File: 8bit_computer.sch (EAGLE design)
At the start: 48 parts, among them IC1 74LS32N, IC10 74LS04N, IC11 74LS04N, IC12 74LS04N, IC13 74LS04N, IC14 74LS08N, IC15 74LS32N, IC16 74LS04N, IC17 74LS86N, IC18 74LS86N, IC19 74LS32N, IC2 74LS04N, IC21 74LS08N, IC22 74LS08N, IC23 74LS32N, IC25 74LS08N, IC26 74LS32N, IC3 74LS08N, IC32 74LS08N, IC33 74LS32N, IC34 74LS245N, IC4 74LS08N, IC5 74LS32N, IC6 74LS04N, IC7 74LS08N, IC8 74LS32N, IC9 74LS04N, Q1 BC556, Q2 BS170

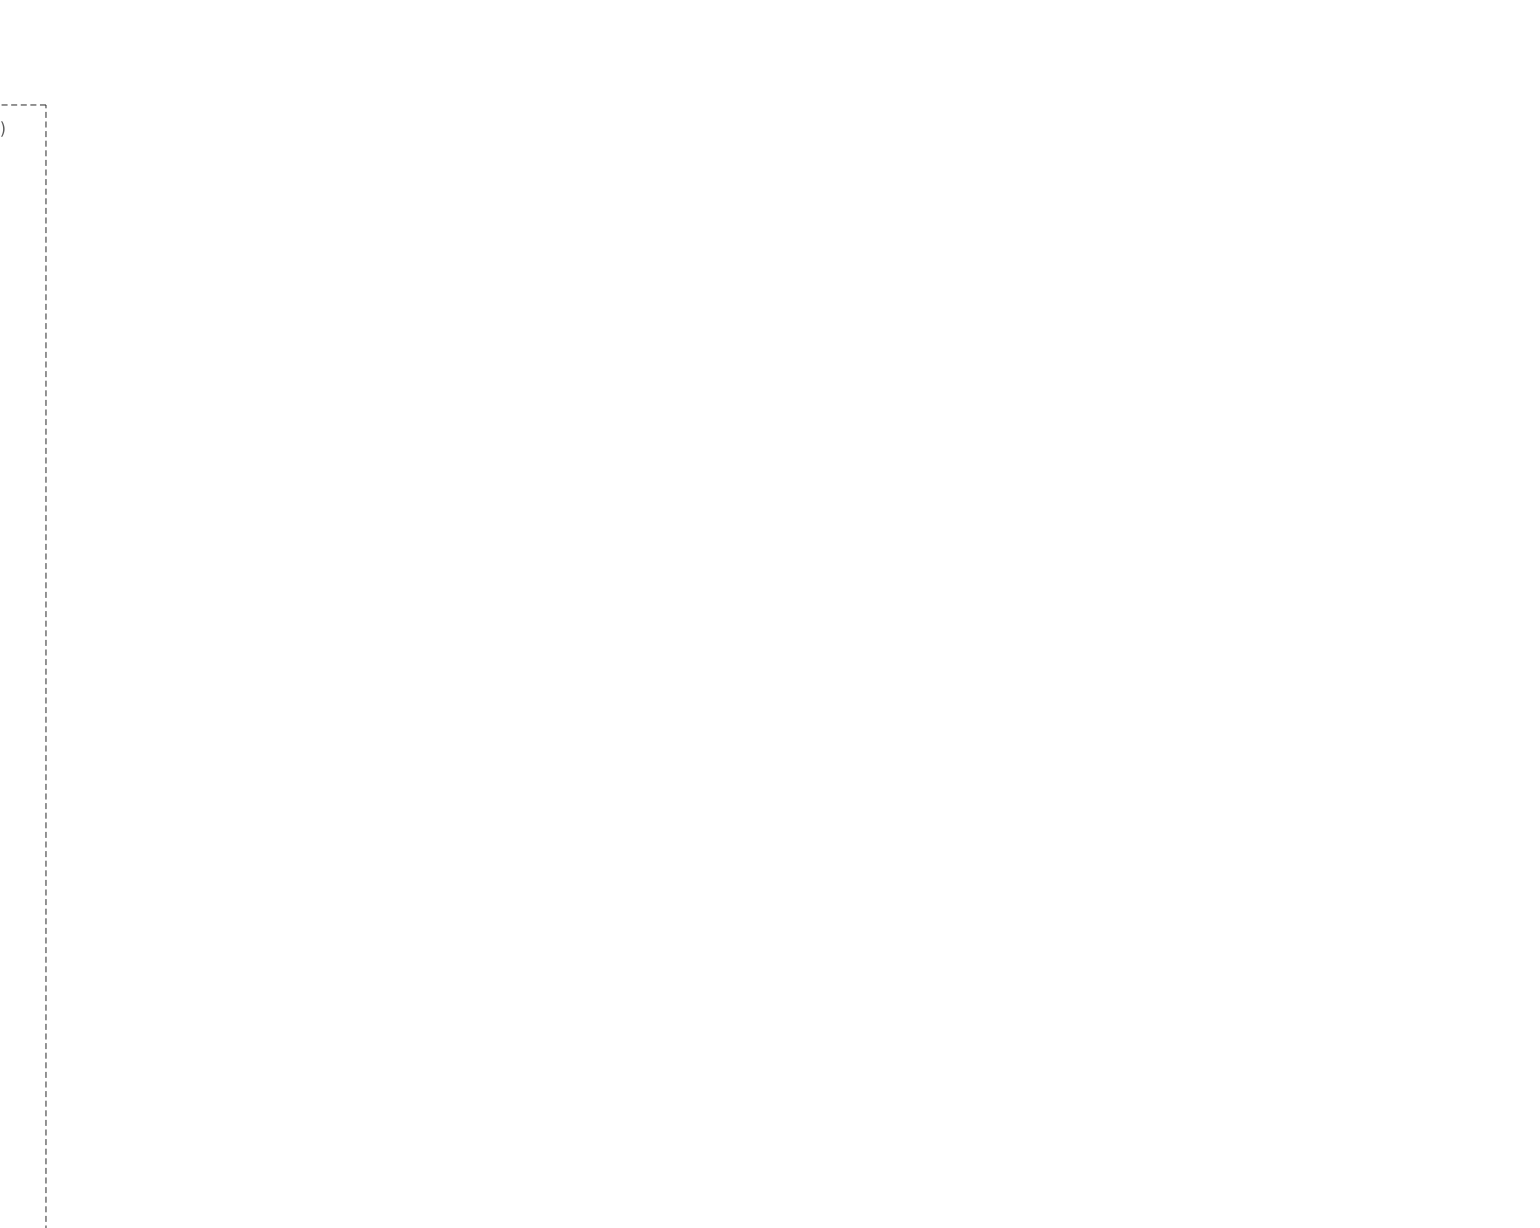
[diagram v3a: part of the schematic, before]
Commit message: Added initial version of SRAM circuit
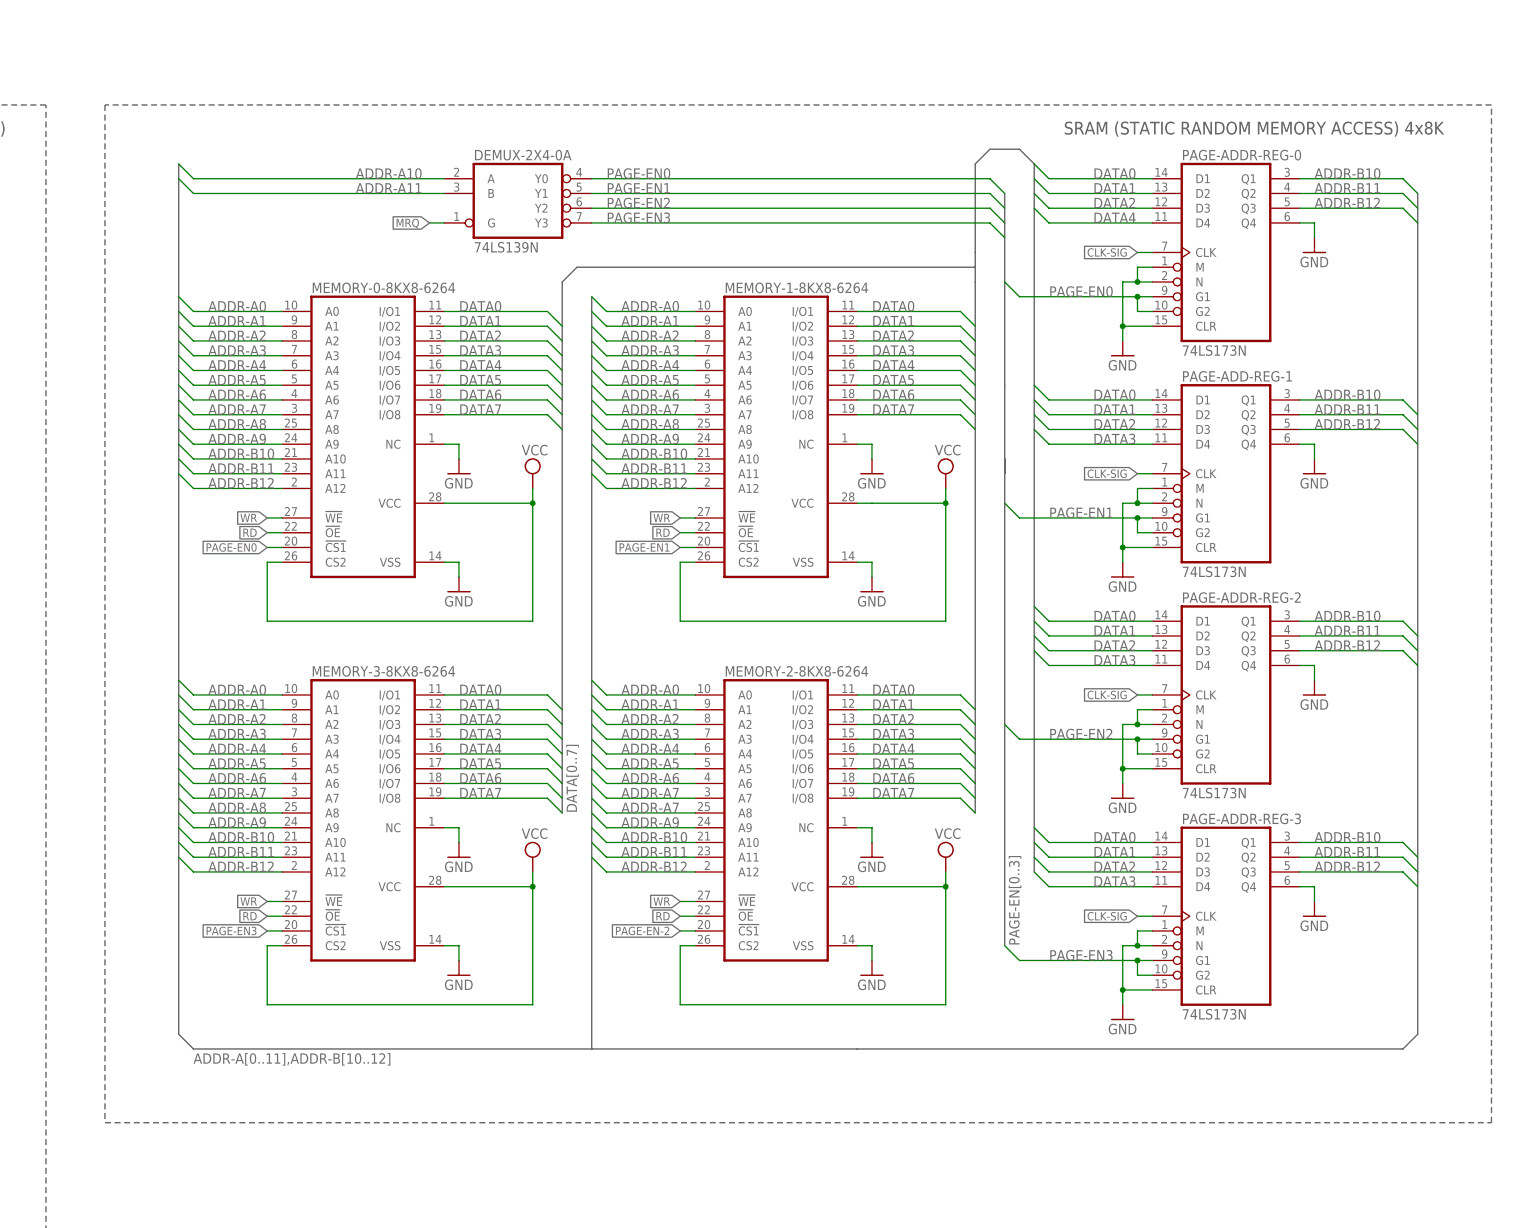
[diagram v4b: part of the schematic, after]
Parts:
- added DEMUX-2X4-0: 74LS139N, 74xx-eu:74LS139N
- added MEMORY-0-8KX8-6264, MEMORY-1-8KX8-6264, MEMORY-2-8KX8-6264, MEMORY-3-8KX8-6264: (no value), memory-hitachi:6264A
- added PAGE-ADD-REG-1, PAGE-ADDR-REG-0, PAGE-ADDR-REG-2, PAGE-ADDR-REG-3: 74LS173N, 74xx-eu:74LS173N
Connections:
- new net ADDR-A0: MEMORY-0-8KX8-6264.A0, MEMORY-1-8KX8-6264.A0, MEMORY-2-8KX8-6264.A0, MEMORY-3-8KX8-6264.A0
- new net ADDR-A1: MEMORY-0-8KX8-6264.A1, MEMORY-1-8KX8-6264.A1, MEMORY-2-8KX8-6264.A1, MEMORY-3-8KX8-6264.A1
- new net ADDR-A10: DEMUX-2X4-0A.A
- new net ADDR-A11: DEMUX-2X4-0A.B
- new net ADDR-A2: MEMORY-0-8KX8-6264.A2, MEMORY-1-8KX8-6264.A2, MEMORY-2-8KX8-6264.A2, MEMORY-3-8KX8-6264.A2
- new net ADDR-A3: MEMORY-0-8KX8-6264.A3, MEMORY-1-8KX8-6264.A3, MEMORY-2-8KX8-6264.A3, MEMORY-3-8KX8-6264.A3
- new net ADDR-A4: MEMORY-0-8KX8-6264.A4, MEMORY-1-8KX8-6264.A4, MEMORY-2-8KX8-6264.A4, MEMORY-3-8KX8-6264.A4
- new net ADDR-A5: MEMORY-0-8KX8-6264.A5, MEMORY-1-8KX8-6264.A5, MEMORY-2-8KX8-6264.A5, MEMORY-3-8KX8-6264.A5
- new net ADDR-A6: MEMORY-0-8KX8-6264.A6, MEMORY-1-8KX8-6264.A6, MEMORY-2-8KX8-6264.A6, MEMORY-3-8KX8-6264.A6
- new net ADDR-A7: MEMORY-0-8KX8-6264.A7, MEMORY-1-8KX8-6264.A7, MEMORY-2-8KX8-6264.A7, MEMORY-2-8KX8-6264.A8, MEMORY-3-8KX8-6264.A7
- new net ADDR-A8: MEMORY-0-8KX8-6264.A8, MEMORY-1-8KX8-6264.A8, MEMORY-3-8KX8-6264.A8
- new net ADDR-A9: MEMORY-0-8KX8-6264.A9, MEMORY-1-8KX8-6264.A9, MEMORY-2-8KX8-6264.A9, MEMORY-3-8KX8-6264.A9
- new net ADDR-B10: MEMORY-0-8KX8-6264.A10, MEMORY-1-8KX8-6264.A10, MEMORY-2-8KX8-6264.A10, MEMORY-3-8KX8-6264.A10, PAGE-ADD-REG-1A.Q1, PAGE-ADDR-REG-0A.Q1, PAGE-ADDR-REG-2A.Q1, PAGE-ADDR-REG-3A.Q1
- new net ADDR-B11: MEMORY-0-8KX8-6264.A11, MEMORY-1-8KX8-6264.A11, MEMORY-2-8KX8-6264.A11, MEMORY-3-8KX8-6264.A11, PAGE-ADD-REG-1A.Q2, PAGE-ADDR-REG-0A.Q2, PAGE-ADDR-REG-2A.Q2, PAGE-ADDR-REG-3A.Q2
- new net ADDR-B12: MEMORY-0-8KX8-6264.A12, MEMORY-1-8KX8-6264.A12, MEMORY-2-8KX8-6264.A12, MEMORY-3-8KX8-6264.A12, PAGE-ADD-REG-1A.Q3, PAGE-ADDR-REG-0A.Q3, PAGE-ADDR-REG-2A.Q3, PAGE-ADDR-REG-3A.Q3
- new net CLK-SIG: PAGE-ADD-REG-1A.CLK, PAGE-ADDR-REG-0A.CLK, PAGE-ADDR-REG-2A.CLK, PAGE-ADDR-REG-3A.CLK
- new net DATA0: MEMORY-0-8KX8-6264.I/O1, MEMORY-1-8KX8-6264.I/O1, MEMORY-2-8KX8-6264.I/O1, MEMORY-3-8KX8-6264.I/O1, PAGE-ADD-REG-1A.D1, PAGE-ADDR-REG-0A.D1, PAGE-ADDR-REG-2A.D1, PAGE-ADDR-REG-3A.D1
- new net DATA1: MEMORY-0-8KX8-6264.I/O2, MEMORY-1-8KX8-6264.I/O2, MEMORY-2-8KX8-6264.I/O2, MEMORY-3-8KX8-6264.I/O2, PAGE-ADD-REG-1A.D2, PAGE-ADDR-REG-0A.D2, PAGE-ADDR-REG-2A.D2, PAGE-ADDR-REG-3A.D2
- new net DATA2: MEMORY-0-8KX8-6264.I/O3, MEMORY-1-8KX8-6264.I/O3, MEMORY-2-8KX8-6264.I/O3, MEMORY-3-8KX8-6264.I/O3, PAGE-ADD-REG-1A.D3, PAGE-ADDR-REG-0A.D3, PAGE-ADDR-REG-2A.D3, PAGE-ADDR-REG-3A.D3
- new net DATA3: MEMORY-0-8KX8-6264.I/O4, MEMORY-1-8KX8-6264.I/O4, MEMORY-2-8KX8-6264.I/O4, MEMORY-3-8KX8-6264.I/O4, PAGE-ADD-REG-1A.D4, PAGE-ADDR-REG-2A.D4, PAGE-ADDR-REG-3A.D4
- new net DATA4: MEMORY-0-8KX8-6264.I/O5, MEMORY-1-8KX8-6264.I/O5, MEMORY-2-8KX8-6264.I/O5, MEMORY-3-8KX8-6264.I/O5, PAGE-ADDR-REG-0A.D4
- new net DATA5: MEMORY-0-8KX8-6264.I/O6, MEMORY-1-8KX8-6264.I/O6, MEMORY-2-8KX8-6264.I/O6, MEMORY-3-8KX8-6264.I/O6
- new net DATA6: MEMORY-0-8KX8-6264.I/O7, MEMORY-1-8KX8-6264.I/O7, MEMORY-2-8KX8-6264.I/O7, MEMORY-3-8KX8-6264.I/O7
- new net DATA7: MEMORY-0-8KX8-6264.I/O8, MEMORY-1-8KX8-6264.I/O8, MEMORY-2-8KX8-6264.I/O8, MEMORY-3-8KX8-6264.I/O8
- new net MRQ: DEMUX-2X4-0A.G
- new net PAGE-EN-2: MEMORY-2-8KX8-6264.!CS1
- new net PAGE-EN0: DEMUX-2X4-0A.Y0, MEMORY-0-8KX8-6264.!CS1, PAGE-ADDR-REG-0A.G1, PAGE-ADDR-REG-0A.G2
- new net PAGE-EN1: DEMUX-2X4-0A.Y1, MEMORY-1-8KX8-6264.!CS1, PAGE-ADD-REG-1A.G1, PAGE-ADD-REG-1A.G2
- new net PAGE-EN2: DEMUX-2X4-0A.Y2, PAGE-ADDR-REG-2A.G1, PAGE-ADDR-REG-2A.G2
- new net PAGE-EN3: DEMUX-2X4-0A.Y3, MEMORY-3-8KX8-6264.!CS1, PAGE-ADDR-REG-3A.G1, PAGE-ADDR-REG-3A.G2
- new net RD: MEMORY-0-8KX8-6264.!OE, MEMORY-1-8KX8-6264.!OE, MEMORY-2-8KX8-6264.!OE, MEMORY-3-8KX8-6264.!OE
- new net WR: MEMORY-0-8KX8-6264.!WE, MEMORY-1-8KX8-6264.!WE, MEMORY-2-8KX8-6264.!WE, MEMORY-3-8KX8-6264.!WE
- net GND: now also MEMORY-0-8KX8-6264.NC, MEMORY-0-8KX8-6264.VSS, MEMORY-1-8KX8-6264.NC, MEMORY-1-8KX8-6264.VSS, MEMORY-2-8KX8-6264.NC, MEMORY-2-8KX8-6264.VSS, MEMORY-3-8KX8-6264.NC, MEMORY-3-8KX8-6264.VSS, PAGE-ADD-REG-1A.CLR, PAGE-ADD-REG-1A.M, PAGE-ADD-REG-1A.N, PAGE-ADD-REG-1A.Q4, PAGE-ADDR-REG-0A.CLR, PAGE-ADDR-REG-0A.M, PAGE-ADDR-REG-0A.N, PAGE-ADDR-REG-0A.Q4, PAGE-ADDR-REG-2A.CLR, PAGE-ADDR-REG-2A.M, PAGE-ADDR-REG-2A.N, PAGE-ADDR-REG-2A.Q4, PAGE-ADDR-REG-3A.CLR, PAGE-ADDR-REG-3A.M, PAGE-ADDR-REG-3A.N, PAGE-ADDR-REG-3A.Q4
- net VCC: now also MEMORY-0-8KX8-6264.CS2, MEMORY-0-8KX8-6264.VCC, MEMORY-1-8KX8-6264.CS2, MEMORY-1-8KX8-6264.VCC, MEMORY-2-8KX8-6264.CS2, MEMORY-2-8KX8-6264.VCC, MEMORY-3-8KX8-6264.CS2, MEMORY-3-8KX8-6264.VCC
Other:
- note added: "SRAM (STATIC RANDOM MEMORY ACCESS) 4x8K"

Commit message: Group ALU mux ifaces into the bus
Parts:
- removed IC10, IC11, IC12, IC13, IC16, IC9: 74LS04N, 74xx-eu:74LS04N
- removed IC17, IC18: 74LS86N, 74xx-eu:74LS86N
- added IC35, IC39, IC42: 74LS32N, 74xx-eu:74LS32N
- added IC37, IC38, IC41: 74LS08N, 74xx-eu:74LS08N
- added IC46, IC47: 74LS86N, 74xx-eu:74LS86N
- IC1, IC5, IC8: value 74LS32N -> 74LS04N; device 74xx-eu:74LS32N -> 74xx-eu:74LS04N
- IC3, IC4, IC7: value 74LS08N -> 74LS04N; device 74xx-eu:74LS08N -> 74xx-eu:74LS04N
- renumbered 4BIT-FULL-ADDER-0 to 4BIT-FULL-ADDER-2, 4BIT-FULL-ADDER-1 to 4BIT-FULL-ADDER-3, IC14 to IC44, IC15 to IC45, IC19 to IC48, IC21 to IC50, IC22 to IC51, IC23 to IC52, IC25 to IC54, IC26 to IC55, IC32 to IC57, IC33 to IC58, IC34 to IC59
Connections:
- net MUX0-1C0-IN renamed MUX0-1C0
- net MUX0-2C0-IN renamed MUX0-2C0
- net MUX0-2C2-IN renamed MUX0-2C2
- net MUX1-1C0-IN renamed MUX1-1C0
- net MUX1-2C0-IN renamed MUX1-2C0
- net MUX2-1C0-IN renamed MUX2-1C0
- net MUX2-1C1-IN renamed MUX2-1C1
- net MUX2-1C3-IN renamed MUX2-1C3
- net MUX2-2C0-IN renamed MUX2-2C0
- net MUX2-2C1-IN renamed MUX2-2C1
- net MUX2-2C3-IN renamed MUX2-2C3
- net MUX3-1C0-IN renamed MUX3-1C0
- net MUX3-1C1-IN renamed MUX3-1C1
- net MUX3-1C3-IN renamed MUX3-1C3
- net MUX3-2C0-IN renamed MUX3-2C0
- net MUX4-2C1-IN renamed MUX3-2C1
- net MUX4-2C3-IN renamed MUX3-2C3
- removed net MUX0-1C1-IN: DUAL-4X1-MUX-0A.1C1, IC1D.O
- removed net MUX0-1C2-IN: DUAL-4X1-MUX-0A.1C2, IC9A.O
- removed net MUX0-1C3-IN: DUAL-4X1-MUX-0A.1C3, IC3D.O
- removed net MUX0-2C1-IN: DUAL-4X1-MUX-0A.2C1, IC5A.O
- removed net MUX0-2C3-IN: DUAL-4X1-MUX-0A.2C3, IC4A.O
- removed net MUX1-1C1-IN: DUAL-4X1-MUX-1A.1C1, IC8D.O
- removed net MUX1-1C2-IN: DUAL-4X1-MUX-1A.1C2, IC6A.O
- removed net MUX1-1C3-IN: DUAL-4X1-MUX-1A.1C3, IC7D.O
- removed net MUX2-1C2-IN: DUAL-4X1-MUX-2A.1C2, IC11A.O
- removed net MUX2-2C2-IN: DUAL-4X1-MUX-2A.2C2, IC12A.O
- removed net MUX3-1C2-IN: DUAL-4X1-MUX-3A.1C2, IC13A.O
- removed net MUX4-2C2-IN: DUAL-4X1-MUX-3A.2C2, IC16A.O
- new net MUX0-1C1: DUAL-4X1-MUX-0A.1C1, IC35D.O
- new net MUX0-1C2: DUAL-4X1-MUX-0A.1C2, IC1A.O
- new net MUX0-1C3: DUAL-4X1-MUX-0A.1C3, IC37D.O
- new net MUX0-2C1: DUAL-4X1-MUX-0A.2C1, IC39A.O
- new net MUX0-2C3: DUAL-4X1-MUX-0A.2C3, IC38A.O
- new net MUX1-1C1: DUAL-4X1-MUX-1A.1C1, IC42D.O
- new net MUX1-1C2: DUAL-4X1-MUX-1A.1C2, IC3A.O
- new net MUX1-1C3: DUAL-4X1-MUX-1A.1C3, IC41D.O
- new net MUX1-2C1: DUAL-4X1-MUX-1A.2C1
- new net MUX1-2C2: DUAL-4X1-MUX-1A.2C2
- new net MUX1-2C3: DUAL-4X1-MUX-1A.2C3
- new net MUX2-1C2: DUAL-4X1-MUX-2A.1C2, IC5A.O
- new net MUX2-2C2: DUAL-4X1-MUX-2A.2C2, IC6A.O
- new net MUX3-1C2: DUAL-4X1-MUX-3A.1C2, IC7A.O
- new net MUX3-2C2: DUAL-4X1-MUX-3A.2C2, IC8A.O
- net ADD0-A0-IN: now also IC46A.O; no longer IC17A.O
- net ADD0-A1-IN: now also IC46B.O; no longer IC17B.O
- net ADD0-A2-IN: now also IC46C.O; no longer IC17C.O
- net ADD0-A3-IN: now also IC46D.O; no longer IC17D.O
- net ADD1-A4-IN: now also IC47A.O; no longer IC18A.O
- net ADD1-A5-IN: now also IC47B.O; no longer IC18B.O
- net ADD1-A6-IN: now also IC47C.O; no longer IC18C.O
- net ADD1-A7-IN: now also IC47D.O; no longer IC18D.O
- net ALU-A0-IN: now also IC1A.I, IC35D.I1, IC37D.I0, IC46A.I1; no longer IC17A.I1, IC1D.I1, IC3D.I0, IC9A.I
- net ALU-A1-IN: now also IC38A.I0, IC39A.I1, IC46B.I1; no longer IC17B.I1, IC4A.I0, IC5A.I1
- net ALU-A2-IN: now also IC3A.I, IC41D.I0, IC42D.I1, IC46C.I1; no longer IC17C.I1, IC6A.I, IC7D.I0, IC8D.I1
- net ALU-A3-IN: now also IC46D.I1, IC4A.I; no longer IC10A.I, IC17D.I1
- net ALU-A4-IN: now also IC47A.I1, IC5A.I; no longer IC11A.I, IC18A.I1
- net ALU-A5-IN: now also IC47B.I1, IC6A.I; no longer IC12A.I, IC18B.I1
- net ALU-A6-IN: now also IC47C.I1, IC7A.I; no longer IC13A.I, IC18C.I1
- net ALU-A7-IN: now also IC47D.I1, IC8A.I; no longer IC16A.I, IC18D.I1
- net ALU-B0-IN: now also IC35D.I0, IC37D.I1; no longer IC1D.I0, IC3D.I1
- net ALU-B1-IN: now also IC38A.I1, IC39A.I0; no longer IC4A.I1, IC5A.I0
- net ALU-B2-IN: now also IC41D.I1, IC42D.I0; no longer IC7D.I1, IC8D.I0
- net C: now also IC46A.I0, IC46B.I0, IC46C.I0, IC46D.I0, IC47A.I0, IC47B.I0, IC47C.I0, IC47D.I0; no longer IC17A.I0, IC17B.I0, IC17C.I0, IC17D.I0, IC18A.I0, IC18B.I0, IC18C.I0, IC18D.I0
- net MUX1-2C1-IN: no longer DUAL-4X1-MUX-1A.2C1
- net MUX1-2C2-IN: now also IC4A.O; no longer DUAL-4X1-MUX-1A.2C2, IC10A.O
- net MUX1-2C3-IN: no longer DUAL-4X1-MUX-1A.2C3
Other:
- moved on the sheet: DEMUX-2X4-0A, IC4A, IC6A, MEMORY-0-8KX8-6264, MEMORY-1-8KX8-6264, MEMORY-2-8KX8-6264, MEMORY-3-8KX8-6264, PAGE-ADD-REG-1, PAGE-ADDR-REG-0, PAGE-ADDR-REG-2, PAGE-ADDR-REG-3
